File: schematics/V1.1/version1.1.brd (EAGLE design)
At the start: 66 x 45 mm, 102 parts, among them IC1 ADG1604S, IC2 LM317MBSTT3, IC3 AD8610R, IC4 AD8610R, IC5 337IMP, IC6 AD8620R, Q1 16MHz, T1 BC847, T2 BC847, T3 BC847, T4 BC847, X2 BU-SMA-H

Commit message: some more layout
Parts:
- moved R5 67.2 mm to (27.8, 19.4), turned to 0 degrees
- moved R6 61.3 mm to (27.8, 21.1), flipped to the top, turned to 0 degrees
- moved C7 59.5 mm to (24.4, 20.2), turned to 0 degrees
- moved R23 58.9 mm to (45.4, 4.76), flipped to the top, turned to 0 degrees
- moved R22 51.4 mm to (45.4, 6.51), flipped to the top, turned to 0 degrees
- moved C10 47.2 mm to (34.3, 15.9), turned to 90 degrees
- moved C31 41.0 mm to (56.4, 24.8)
- moved C29 38.3 mm to (48.3, 8.89), flipped to the top, turned to 90 degrees
- moved C8 37.4 mm to (16.7, 14.9), turned to 270 degrees
- moved R14 32.9 mm to (53.2, 34.9), turned to 270 degrees
- moved C9 32.5 mm to (31.6, 16.2)
- moved C5 32.1 mm to (29.5, 16.0)
- moved R31 30.6 mm to (36.0, 25.7)
- moved R29 23.0 mm to (37.8, 25.7), flipped to the bottom, turned to 270 degrees
- moved C28 23.0 mm to (29.7, 37.0), flipped to the top, turned to 270 degrees
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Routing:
- net N$11: track 0.00 -> 10.0 mm
- net N$22: track 0.00 -> 8.77 mm, vias 0 -> 1
- net N$36: track 0.00 -> 7.30 mm
- net +3V3: track 0.00 -> 6.92 mm
- net N$53: track 0.00 -> 6.68 mm, vias 0 -> 1
- net VCC: track 92.1 -> 98.6 mm
- net -3V3: track 3.62 -> 9.43 mm
- net N$19: track 0.00 -> 3.85 mm, vias 0 -> 1
- net N$21: track 0.00 -> 1.95 mm, vias 0 -> 1
- net N$12: track 0.00 -> 1.91 mm
- net N$54: track 0.00 -> 1.75 mm
- net N$23: track 0.00 -> 1.59 mm, vias 0 -> 1

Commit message: finalize the v1.1 layout
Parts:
- added C11, C12: 100n, rcl:C0603
- moved C10 20.1 mm to (15.9, 24.0), turned to 315 degrees
- moved C34 18.7 mm to (44.0, 28.9), flipped to the top, turned to 0 degrees
- moved C5 14.3 mm to (19.8, 5.56), flipped to the top
- moved C28 14.1 mm to (16.4, 32.4), turned to 90 degrees
- moved C9 12.2 mm to (21.3, 22.7), turned to 225 degrees
- moved R12 9.56 mm to (51.4, 19.4)
- moved C32 8.99 mm to (48.1, 19.5), flipped to the top, turned to 180 degrees
- moved R13 7.27 mm to (54.6, 19.4)
- moved R14 7.19 mm to (47.0, 31.3), turned to 180 degrees
- moved IC3 1.59 mm to (46.8, 35.4)
- moved R11 1.37 mm to (50.3, 27.8), turned to 180 degrees
- moved C30 1.11 mm to (48.3, 23.5)
- moved R19 0.16 mm to (46.8, 22.9)
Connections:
- net +12V: now also C11.2
- net -12V: now also C12.1
- net AGND: now also C11.1, C12.2
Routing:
- net +12V: track 5.86 -> 80.6 mm, vias 1 -> 4
- net +3V3: track 6.92 -> 66.8 mm, vias 0 -> 4
- net -12V: track 10.2 -> 67.3 mm, vias 1 -> 3
- net -3V3: track 9.43 -> 55.0 mm, vias 1 -> 5
- net N$48: track 6.38 -> 46.0 mm, vias 0 -> 2
- net N$23: track 1.59 -> 39.1 mm
- net N$21: track 1.95 -> 34.5 mm, vias 1 -> 2
- net N$47: track 1.76 -> 33.8 mm, vias 0 -> 1
- net N$49: track 1.76 -> 29.8 mm, vias 0 -> 2
- net N$22: track 8.77 -> 35.7 mm
- net N$18: track 0.00 -> 24.1 mm, vias 0 -> 1
- net N$20: track 0.00 -> 22.5 mm, vias 0 -> 1
- net N$34: track 0.00 -> 21.6 mm, vias 0 -> 1
- net N$46: track 4.28 -> 24.2 mm, vias 0 -> 1
- net N$16: track 7.03 -> 24.5 mm, vias 0 -> 2
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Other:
- board text added: "(c)2015 Hendrik Lüth"
- board text added: "LabConnect Signalgenerator"
- board text added: "github.com/LabConnect"
- board text removed: "(c)2015 Hendrik Lüth LabConnect Signalgenerator github.com/labconnect"

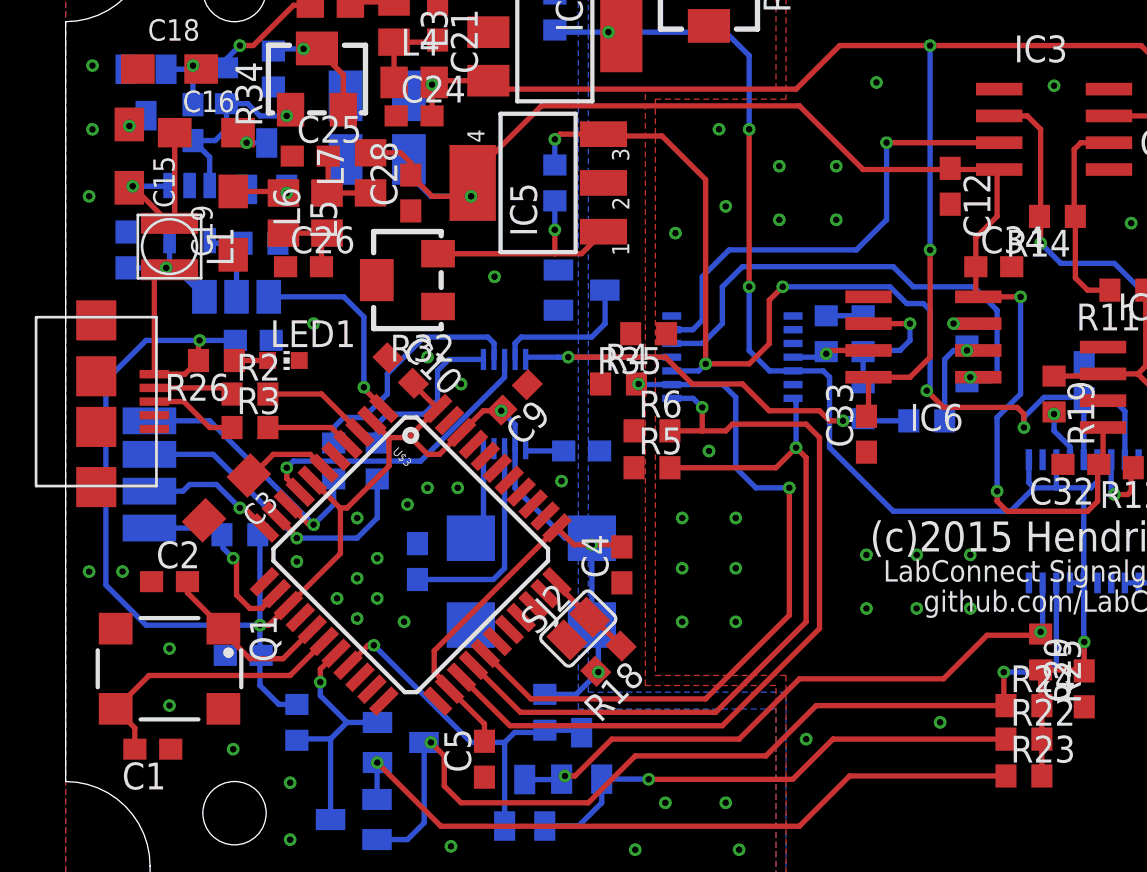
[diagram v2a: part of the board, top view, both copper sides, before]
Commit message: restructure the circuit and pcb-layout to fix the offset issue
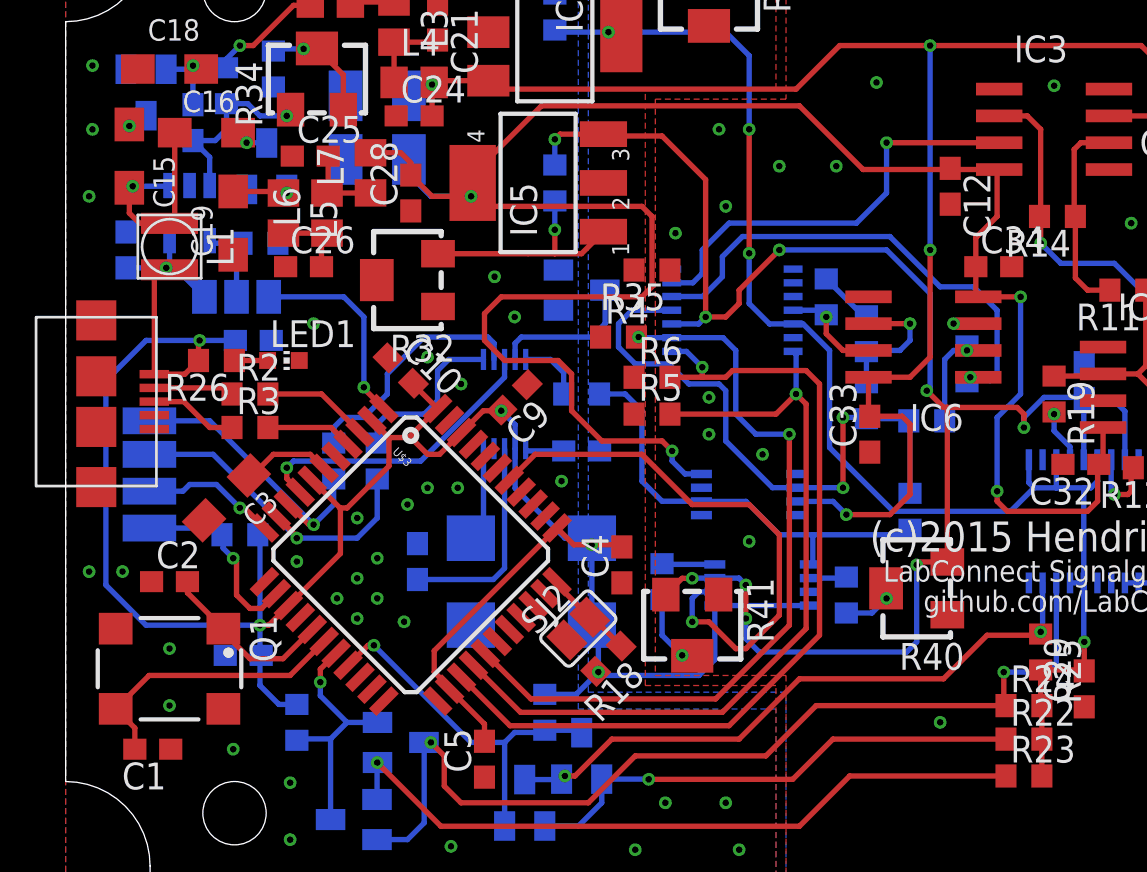
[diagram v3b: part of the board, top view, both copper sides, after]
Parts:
- added IC7: AD8610MR, analog-devices:MSOP08
- added R36, R37, R38, R39: 0R, rcl:R0603
- added R40, R41: 2k, rcl:RTRIM3224W
- added U$12: DG419LDQ, switch:MSOP08
- moved R35 3.02 mm to (27.8, 28.7)
- moved R5 2.54 mm to (27.8, 21.9)
- moved R6 2.54 mm to (27.8, 23.7)
- moved IC1 2.22 mm to (31.6, 26.8)
- moved R4 2.22 mm to (26.2, 25.6)
- moved R31 1.75 mm to (36.0, 27.5)
- moved C33 0.16 mm to (38.1, 21.0)
- moved R29 0.16 mm to (37.9, 25.7)
- moved R30 0.16 mm to (37.9, 22.5)
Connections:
- new net N$58: R36.2, U$1.10
- new net N$59: IC7.2, R36.1, R37.2, U$12.1
- new net N$60: R38.1, U$12.8
- new net N$61: U$12.6, U$3.38
- new net N$62: R39.1, U$12.2
- new net N$63: R39.2, R40.2
- new net N$64: R38.2, R41.2
- net +12V: now also IC7.7
- net -12V: now also IC7.4
- net -3V3: now also R40.3, R41.3, U$12.7
- net AGND: now also IC7.1, IC7.3, IC7.5, R40.1, R41.1, U$12.3
- net N$16: now also IC7.6, R37.1; no longer U$1.10
- net VCC: now also U$12.4, U$12.5
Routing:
- net -12V: track 67.3 -> 103.5 mm, vias 3 -> 4
- net N$61: track 0.00 -> 26.3 mm, vias 0 -> 1
- net -3V3: track 55.0 -> 80.8 mm, vias 5 -> 9
- net N$59: track 0.00 -> 21.0 mm
- net VCC: track 109.7 -> 122.6 mm
- net +12V: track 80.6 -> 92.0 mm, vias 4 -> 5
- net N$16: track 24.5 -> 28.7 mm
- net N$64: track 0.00 -> 3.52 mm, vias 0 -> 1
- net N$58: track 0.00 -> 3.07 mm
- net N$63: track 0.00 -> 2.68 mm, vias 0 -> 1
- net N$60: track 0.00 -> 2.51 mm
- net N$22: track 35.7 -> 38.1 mm
- net N$21: track 34.5 -> 36.7 mm
- net N$23: track 39.1 -> 41.3 mm
- net N$20: track 22.5 -> 20.3 mm
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
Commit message: create the gerber files for V1.1
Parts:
- moved C1 0.95 mm to (3.17, 6.03)
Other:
- board text added: "Seriennummer:"
- board text added: "https://github.com/LabConnect"
- board text removed: "github.com/LabConnect"
